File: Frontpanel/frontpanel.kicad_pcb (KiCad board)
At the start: 2 copper layers, 90 x 148 mm, 13 parts

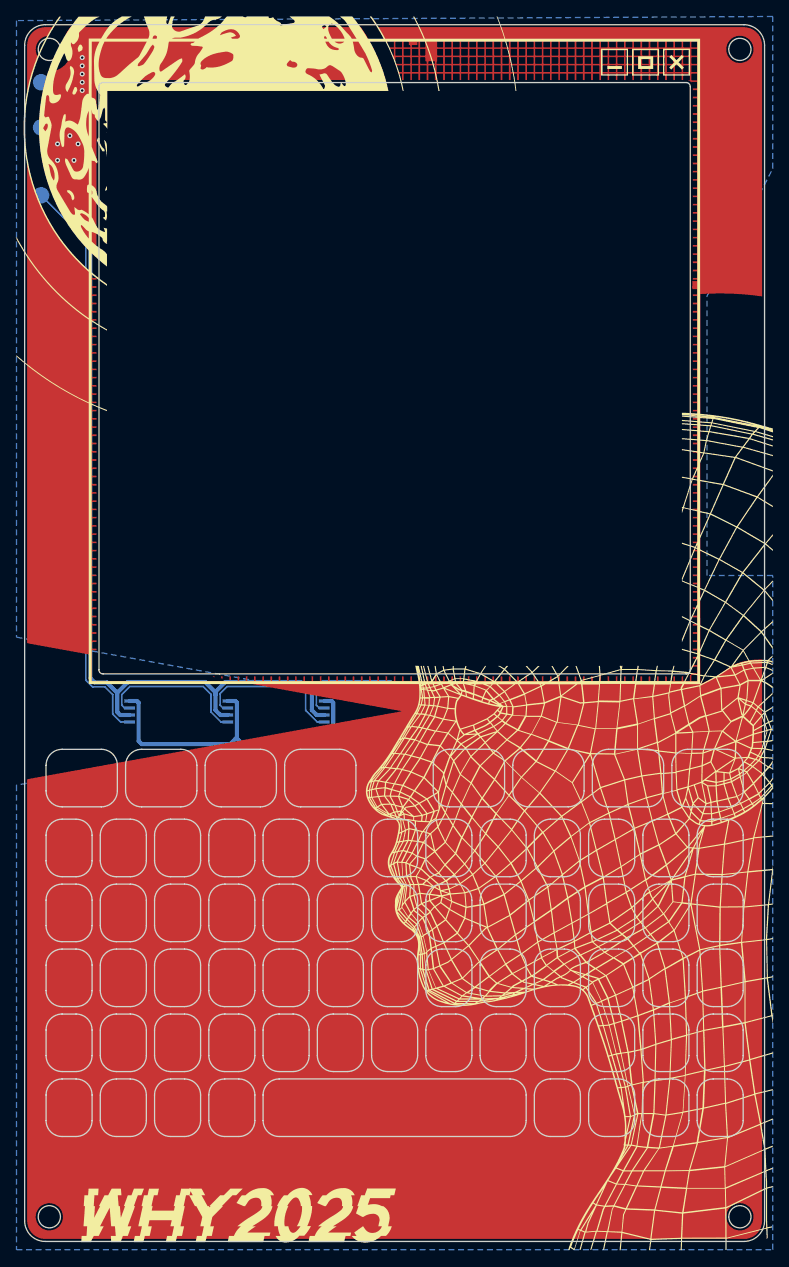
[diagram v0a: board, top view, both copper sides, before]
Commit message: Started ripping parts out
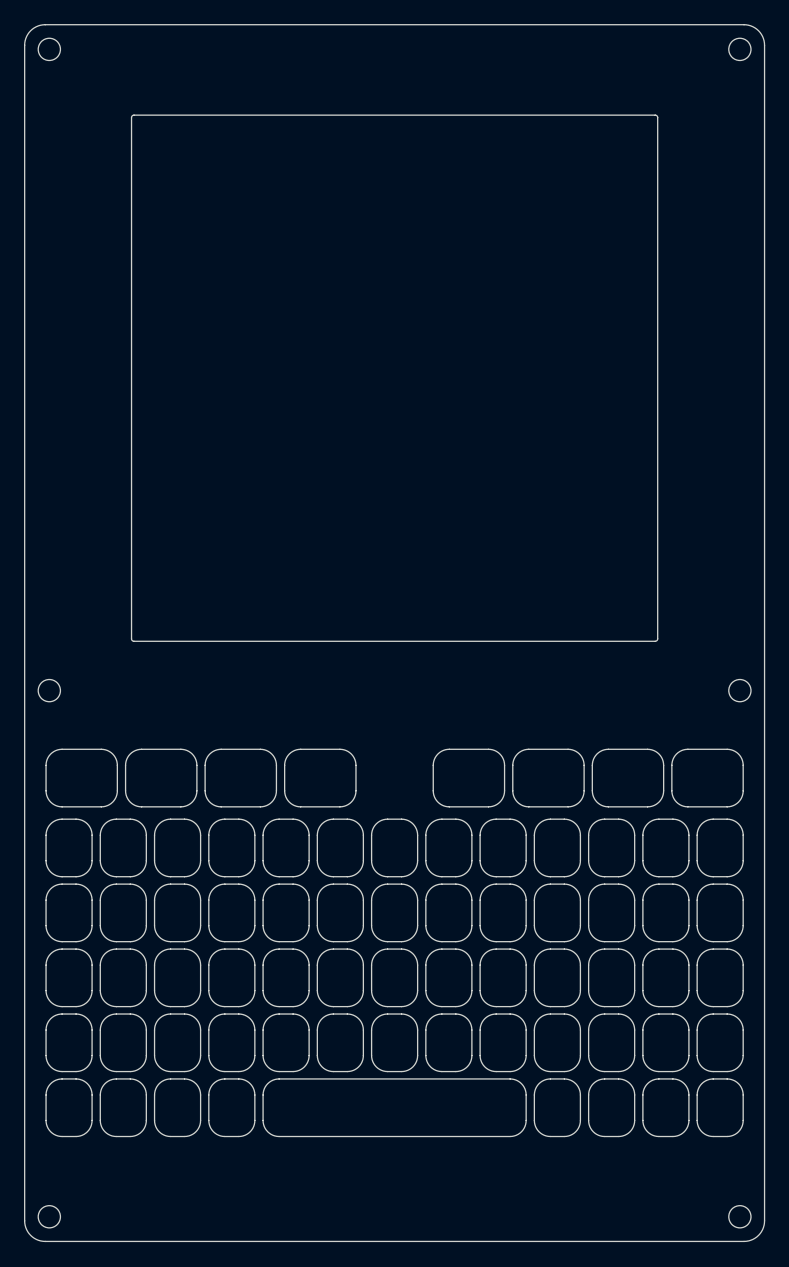
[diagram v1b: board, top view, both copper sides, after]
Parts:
- removed D1, D2, D3, D4: WS2812B-4020, frontpanel:LED_WS2812B-4020
- removed TP1, TP3, TP6: TestPoint, TestPoint:TestPoint_Pad_D2.0mm
- added REF**: MountingHole_2.7mm_M2.5_DIN965, MountingHole:MountingHole_2.7mm_M2.5_DIN965, F.Cu at (117.0, 108.0)
- added REF**: MountingHole_2.7mm_M2.5_DIN965, MountingHole:MountingHole_2.7mm_M2.5_DIN965, F.Cu at (33.0, 108.0)
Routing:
- net 5V: track 132.9 -> 0.00 mm
- net GPIO4: track 70.0 -> 0.00 mm
- net GND: track 34.2 -> 0.00 mm, vias 10 -> 0
- net Net-(D1-DOUT): track 18.7 -> 0.00 mm
- net Net-(D2-DOUT): track 18.5 -> 0.00 mm
- net Net-(D3-DOUT): track 17.8 -> 0.00 mm
- removed copper zone on B.Cu, net GND
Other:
- board text removed: "+3.3"
- board text removed: "+5V"
- board text removed: "1"
- board text removed: "2"
- board text removed: "3.3V"
- board text removed: "5V"
- board text removed: "CRESET"
- board text removed: "GND"
- board text removed: "INT1"
- board text removed: "INT2"
- board text removed: "IO0"
- board text removed: "IO1/DBL"
- board text removed: "IO2"
- board text removed: "IO3"
- board text removed: "IO4"
- board text removed: "RTC"
- board text removed: "SCL"
- board text removed: "SDA"
- board text removed: "STROBE"
- board text removed: "[1] place pogo pins on this location on the carrier board [2] place 4x WS2812B 4020 on these footprints [3] use the WS2812 library to light up your badge"
- board text removed: "a n e n t ?"
- board text removed: "d n e r d W"
- board text removed: "d o v i u Y"
- board text removed: "i y e f o H"
- board text removed: "unlock your frontpanel"
- board text removed: "~{INT_KEY}"
